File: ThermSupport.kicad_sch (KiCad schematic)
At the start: 18 parts, among them J1 855135013

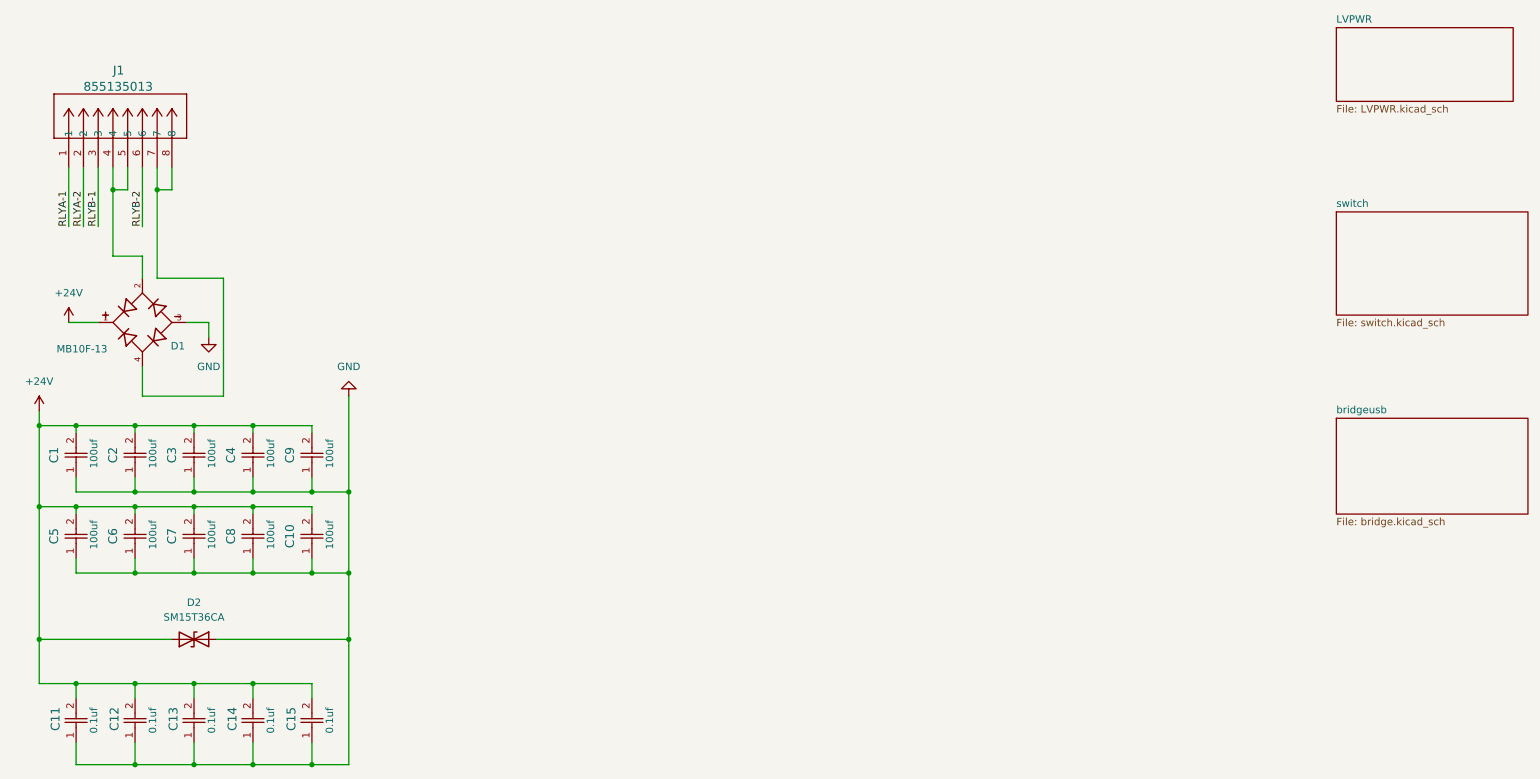
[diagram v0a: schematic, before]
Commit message: Added sensor page plus relays, and additional power
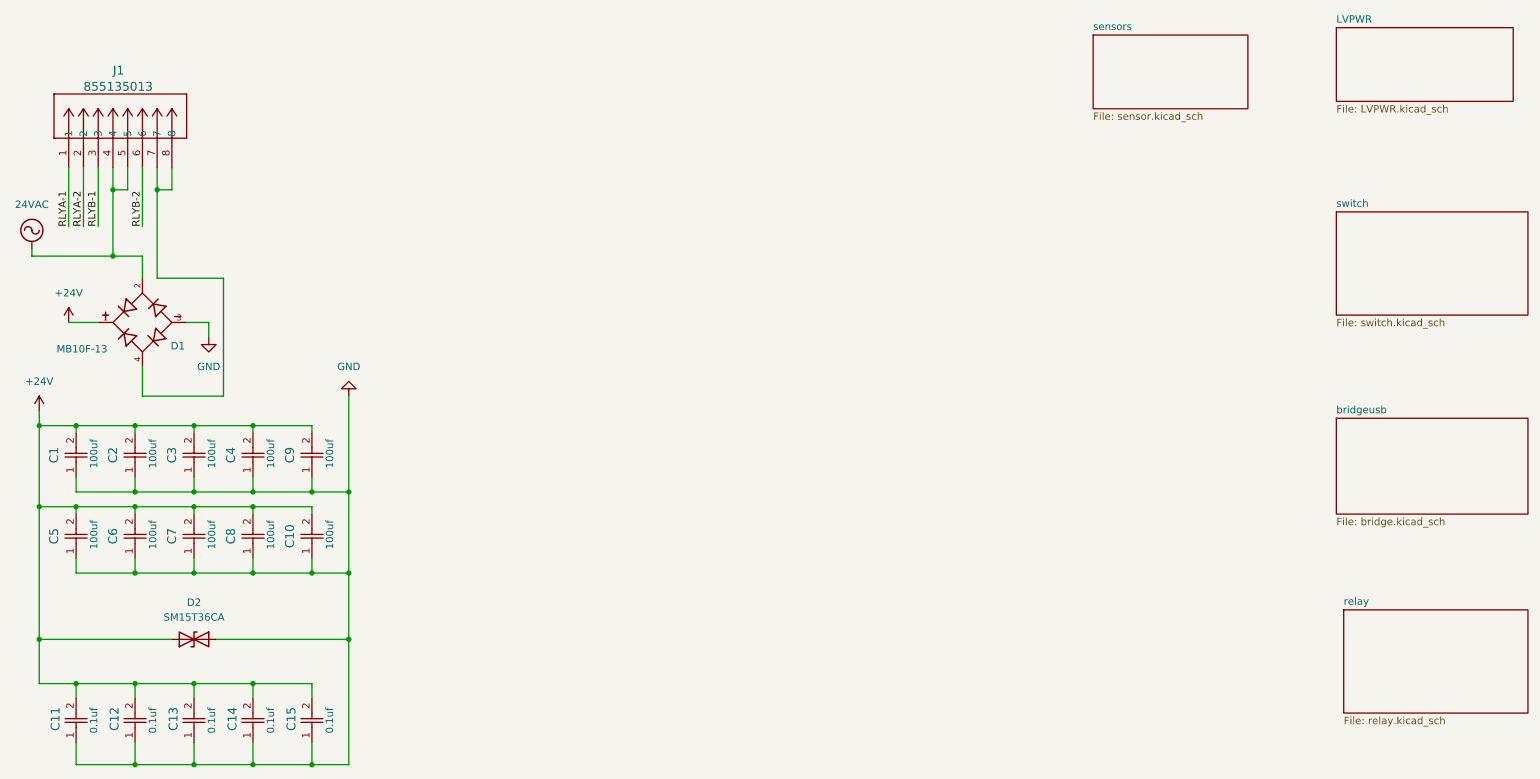
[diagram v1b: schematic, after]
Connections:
- net 24VAC: now reaches D1.2, J1.4, J1.5
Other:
- added sheet relay (relay.kicad_sch)
- added sheet sensors (sensor.kicad_sch)
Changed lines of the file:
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@@
+	)
+	(junction
+		(at 29.21 59.69)
+		(diameter 0)
+		(color 0 0 0 0)
 	)
 	(junction
@@
 	(wire
 		(pts
+			(xy 15.24 59.69) (xy 15.24 58.42)
+		)
+		(stroke
+			(width 0)
+			(type default)
+		)
+	)
+	(wire
+		(pts
 			(xy 69.85 125.73) (xy 46.99 125.73)
+		)
+		(stroke
+			(width 0)
+			(type default)
+		)
+	)
+	(wire
+		(pts
+			(xy 29.21 59.69) (xy 15.24 59.69)
 		)
 		(stroke
@@
 	)
 	(symbol
+		(lib_id "power:AC")
+		(at 15.24 58.42 0)
+		(unit 1)
+		(exclude_from_sim no)
+		(in_bom yes)
+		(on_board yes)
+		(dnp no)
+		(fields_autoplaced yes)
+		(property "Reference" "#PWR051"
+			(at 15.24 60.96 0)
+			(effects
+				(font
+					(size 1.27 1.27)
+				)
+				(hide yes)
+			)
+		)
+		(property "Value" "24VAC"
+			(at 15.24 50.8 0)
+			(effects
+				(font
+					(size 1.27 1.27)
+				)
+			)
+		)
+		(property "Footprint" ""
+			(at 15.24 58.42 0)
+			(effects
+				(font
+					(size 1.27 1.27)
+				)
+				(hide yes)
+			)
+		)
+		(property "Datasheet" ""
+			(at 15.24 58.42 0)
+			(effects
+				(font
+					(size 1.27 1.27)
+				)
+				(hide yes)
+			)
+		)
+		(property "Description" "Power symbol creates a global label with name \"AC\""
+			(at 15.24 58.42 0)
+			(effects
+				(font
+					(size 1.27 1.27)
+				)
+				(hide yes)
+			)
+		)
+		(pin "1"
+		)
+		(instances
+			(project ""
+				(path "/8f4ec0db-d54b-4b4a-bf20-32f8c98f56be"
+					(reference "#PWR051")
+					(unit 1)
+				)
+			)
+		)
+	)
+	(symbol
 		(lib_id "2025-04-20_14-21-47:855135013")
 		(at 21.59 44.45 90)
@@
 	)
 	(sheet
+		(at 198.12 21.59)
+		(size 26.67 12.7)
+		(exclude_from_sim no)
+		(in_bom yes)
+		(on_board yes)
+		(dnp no)
+		(fields_autoplaced yes)
+		(stroke
+			(width 0.1524)
+			(type solid)
+		)
+		(fill
+			(color 0 0 0 0.0000)
+		)
+		(property "Sheetname" "sensors"
+			(at 198.12 20.8784 0)
+			(effects
+				(font
+					(size 1.27 1.27)
+				)
+				(justify left bottom)
+			)
+		)
+		(property "Sheetfile" "sensor.kicad_sch"
+			(at 198.12 34.8746 0)
+			(effects
+				(font
+					(size 1.27 1.27)
+				)
+				(justify left top)
+			)
+		)
+		(instances
+			(project "ThermSupport"
+				(path "/8f4ec0db-d54b-4b4a-bf20-32f8c98f56be"
+					(page "12")
+				)
+			)
+		)
+	)
+	(sheet
 		(at 240.03 52.07)
 		(size 33.02 17.78)
@@
 				)
 			)
+		)
+	)
+	(sheet
+		(at 241.3 120.65)
+		(size 31.75 17.78)
+		(exclude_from_sim no)
+		(in_bom yes)
+		(on_board yes)
+		(dnp no)
+		(fields_autoplaced yes)
+		(stroke
+			(width 0.1524)
+			(type solid)
+		)
+		(fill
+			(color 0 0 0 0.0000)
+		)
+		(property "Sheetname" "relay"
+			(at 241.3 119.9384 0)
+			(effects
+				(font
+					(size 1.27 1.27)
+				)
+				(justify left bottom)
+			)
+		)
+		(property "Sheetfile" "relay.kicad_sch"
+			(at 241.3 139.0146 0)
+			(effects
+				(font
+					(size 1.27 1.27)
+				)
+				(justify left top)
+			)
+		)
+		(instances
+			(project "ThermSupport"
+				(path "/8f4ec0db-d54b-4b4a-bf20-32f8c98f56be"
+					(page "5")
+				)
+			)
